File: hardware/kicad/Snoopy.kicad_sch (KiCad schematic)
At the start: 10 parts, among them J1 JST PH 8-pin male, J2 JST XH 5-pin male, J3 Deans T-Plug Female, J5 JST XH 5-pin male, U1 ESP32 DEV KIT DOIT 30-pin, U2 MH-KC24

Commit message: T Plug fix
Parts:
- J3: value Deans T-Plug Female -> Deans T-Plug Male
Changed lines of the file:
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@@
       (effects (font (size 1.27 1.27)))
     )
-    (property "Value" "Deans T-Plug Female" (at 176.53 133.985 0)
+    (property "Value" "Deans T-Plug Male" (at 176.53 133.985 0)
       (effects (font (size 1.27 1.27)))
     )

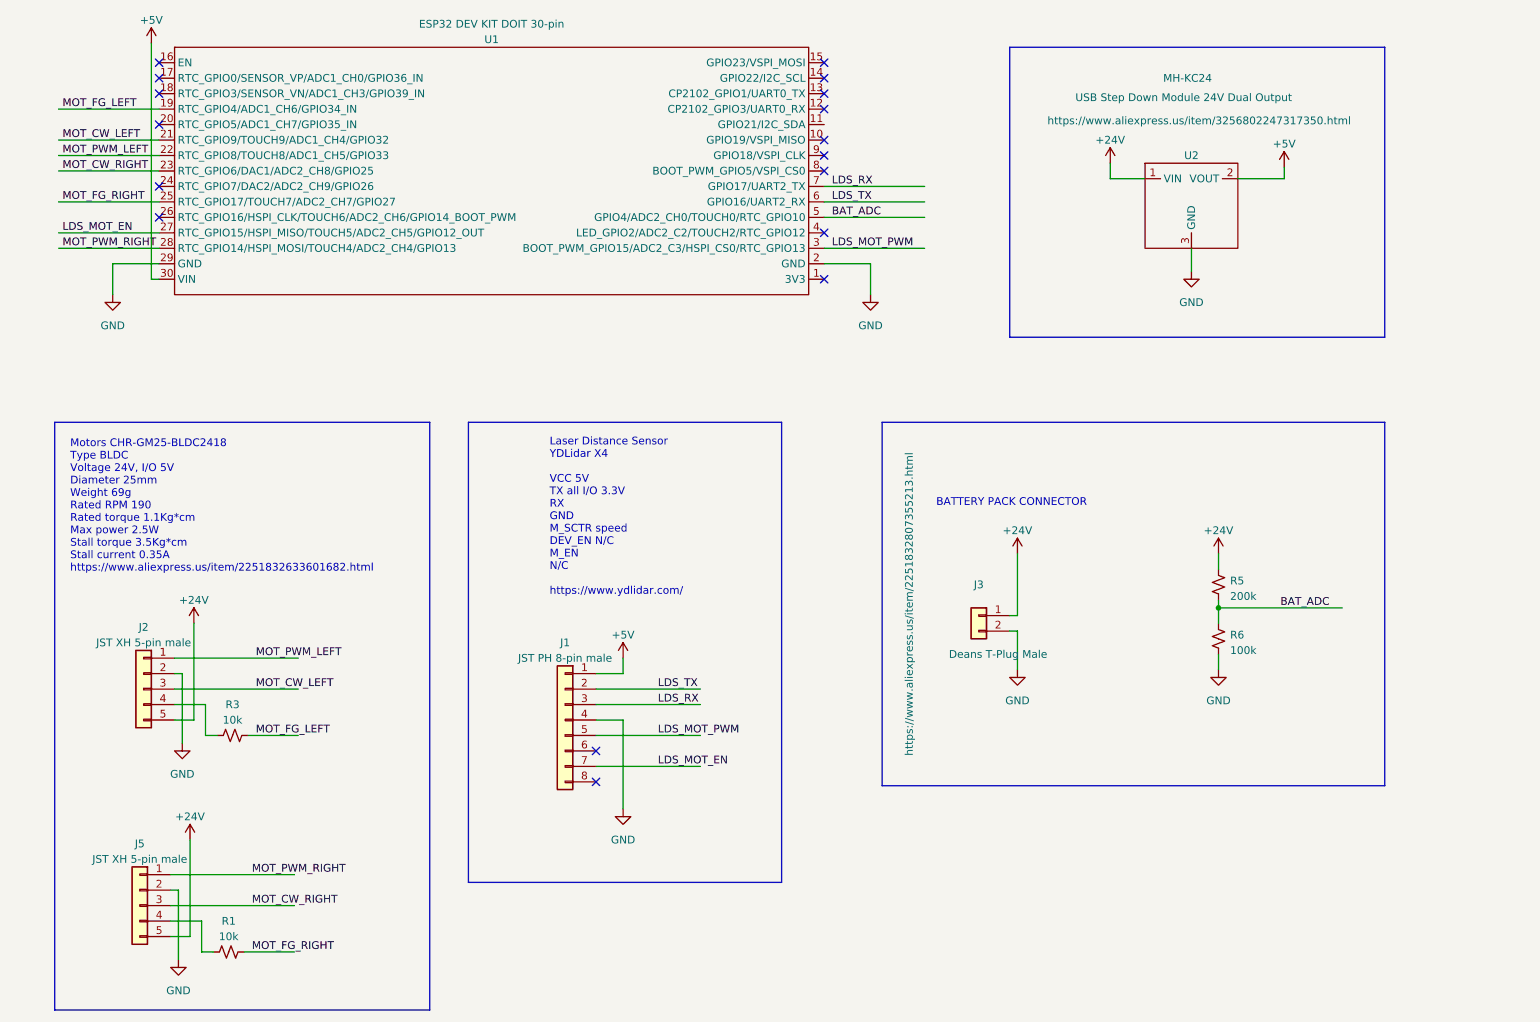
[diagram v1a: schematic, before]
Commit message: Servos, dock, pulldowns
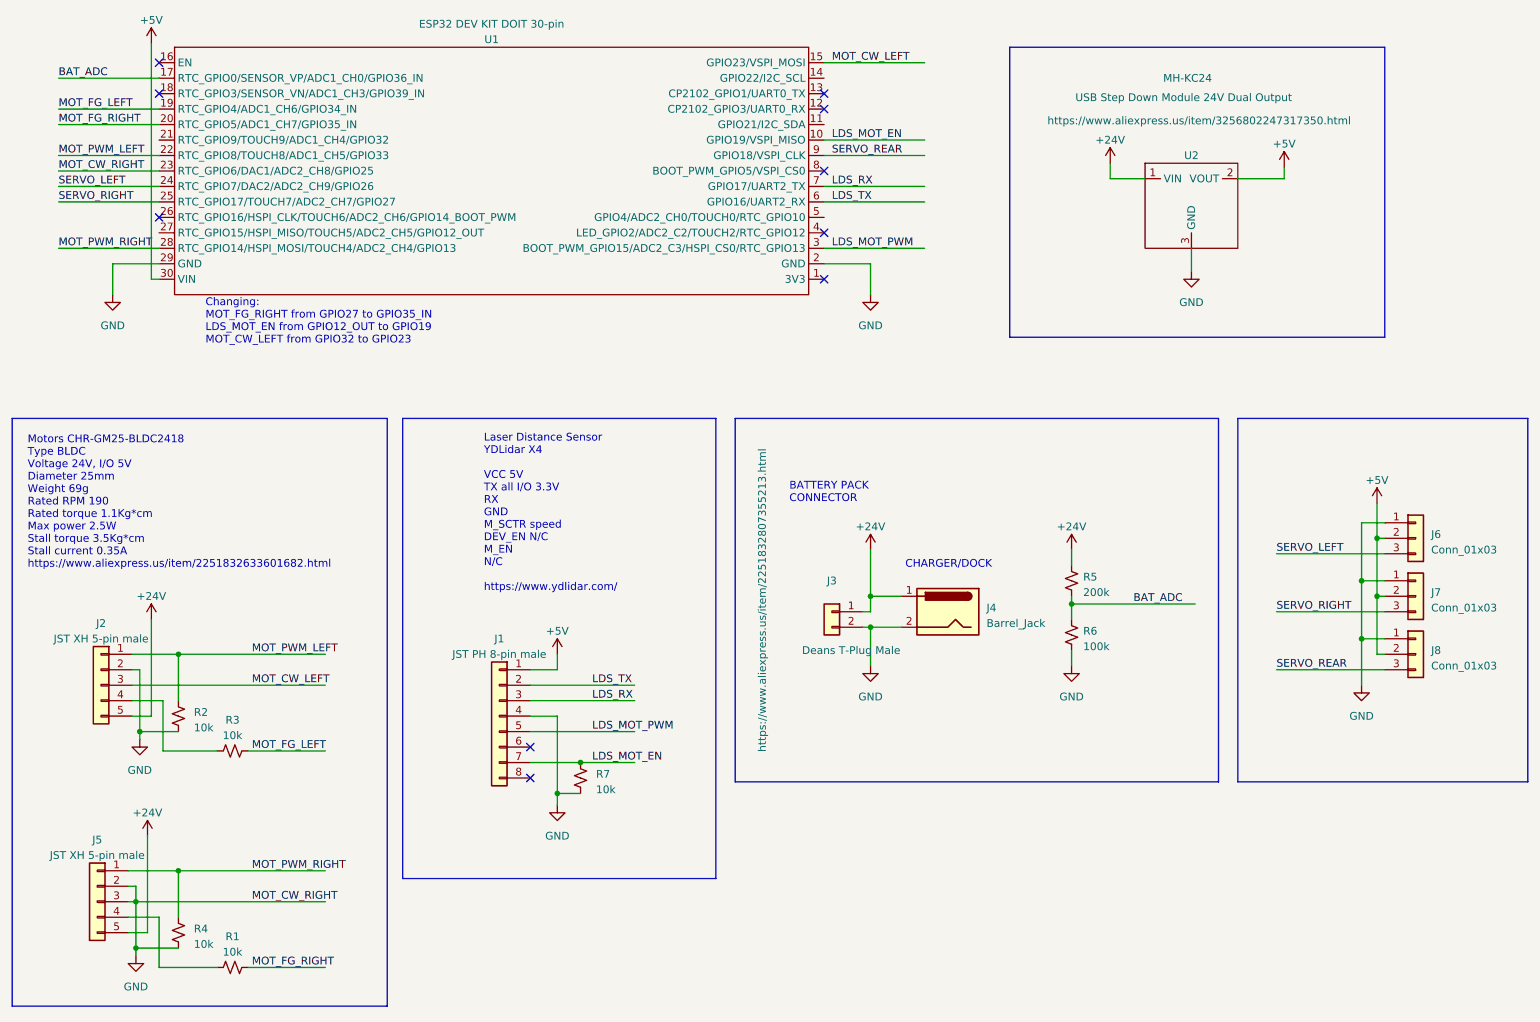
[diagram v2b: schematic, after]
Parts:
- added J4: Barrel_Jack, symbol Connector:Barrel_Jack
- added J6, J7, J8: Conn_01x03, symbol Connector_Generic:Conn_01x03
- added R2, R4, R7: 10k, symbol Device:R_Small_US
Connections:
- net MOT_CW_RIGHT is gone; now on net GND: J5.3 (Pin_3), U1.23 (RTC_GPIO6/DAC1/ADC2_CH8/GPIO25)
- net +24V: now also J4.1
- net +5V: now also J6.2 (Pin_2), J7.2 (Pin_2), J8.2 (Pin_2)
- net BAT_ADC: now also U1.17 (RTC_GPIO0/SENSOR_VP/ADC1_CH0/GPIO36_IN); no longer U1.5 (GPIO4/ADC2_CH0/TOUCH0/RTC_GPIO10)
- net GND: now also J4.2, J6.1 (Pin_1), J7.1 (Pin_1), J8.1 (Pin_1), R2.2, R4.2, R7.2
- net LDS_MOT_EN: now also U1.10 (GPIO19/VSPI_MISO), R7.1; no longer U1.27 (RTC_GPIO15/HSPI_MISO/TOUCH5/ADC2_CH5/GPIO12_OUT)
- net MOT_CW_LEFT: now also U1.15 (GPIO23/VSPI_MOSI); no longer U1.21 (RTC_GPIO9/TOUCH9/ADC1_CH4/GPIO32)
- net MOT_FG_RIGHT: now also U1.20 (RTC_GPIO5/ADC1_CH7/GPIO35_IN); no longer U1.25 (RTC_GPIO17/TOUCH7/ADC2_CH7/GPIO27)
- net MOT_PWM_LEFT: now also R2.1
- net MOT_PWM_RIGHT: now also R4.1
- net SERVO_LEFT: now reaches U1.24 (RTC_GPIO7/DAC2/ADC2_CH9/GPIO26)
- net SERVO_LEFT: now also J6.3 (Pin_3)
- net SERVO_REAR: now reaches U1.9 (GPIO18/VSPI_CLK)
- net SERVO_REAR: now also J8.3 (Pin_3)
- new net SERVO_RIGHT: J7.3 (Pin_3), U1.25 (RTC_GPIO17/TOUCH7/ADC2_CH7/GPIO27)
- no-connect marks 17 -> 10
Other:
- note added: "CHARGER/DOCK"
- note added: "Changing: MOT_FG_RIGHT from GPIO27 to GPIO35_IN LDS_MOT_EN from GPIO12_OUT to GPIO19 MOT_CW_LEFT from GPIO32 to GPIO23"
- moved on the sheet: J1, J2, J3, J5, R1, R3, R5, R6
